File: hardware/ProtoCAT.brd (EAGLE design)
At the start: 59.7 x 53.3 mm, 53 parts, among them U1 ARDUINO

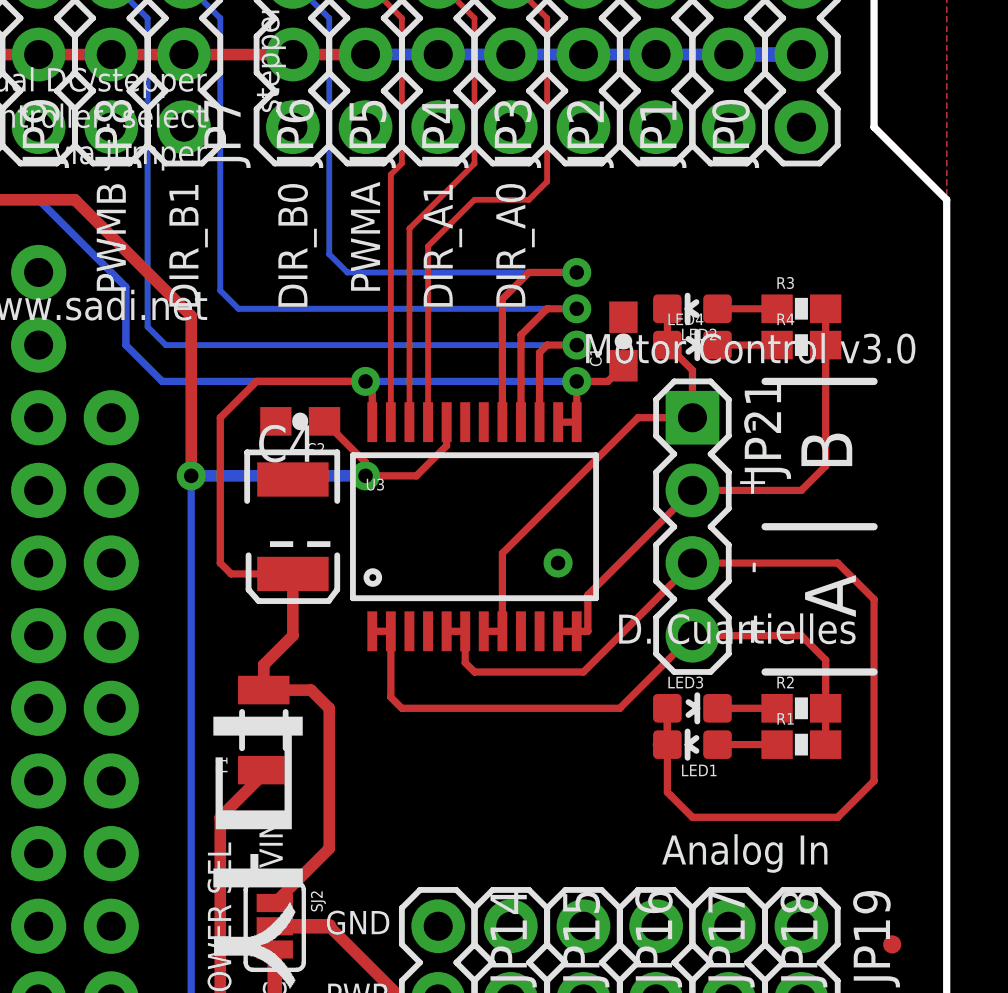
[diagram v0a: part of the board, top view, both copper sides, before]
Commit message: Removed unused layers
Removed unused layers and backup b# / s# files
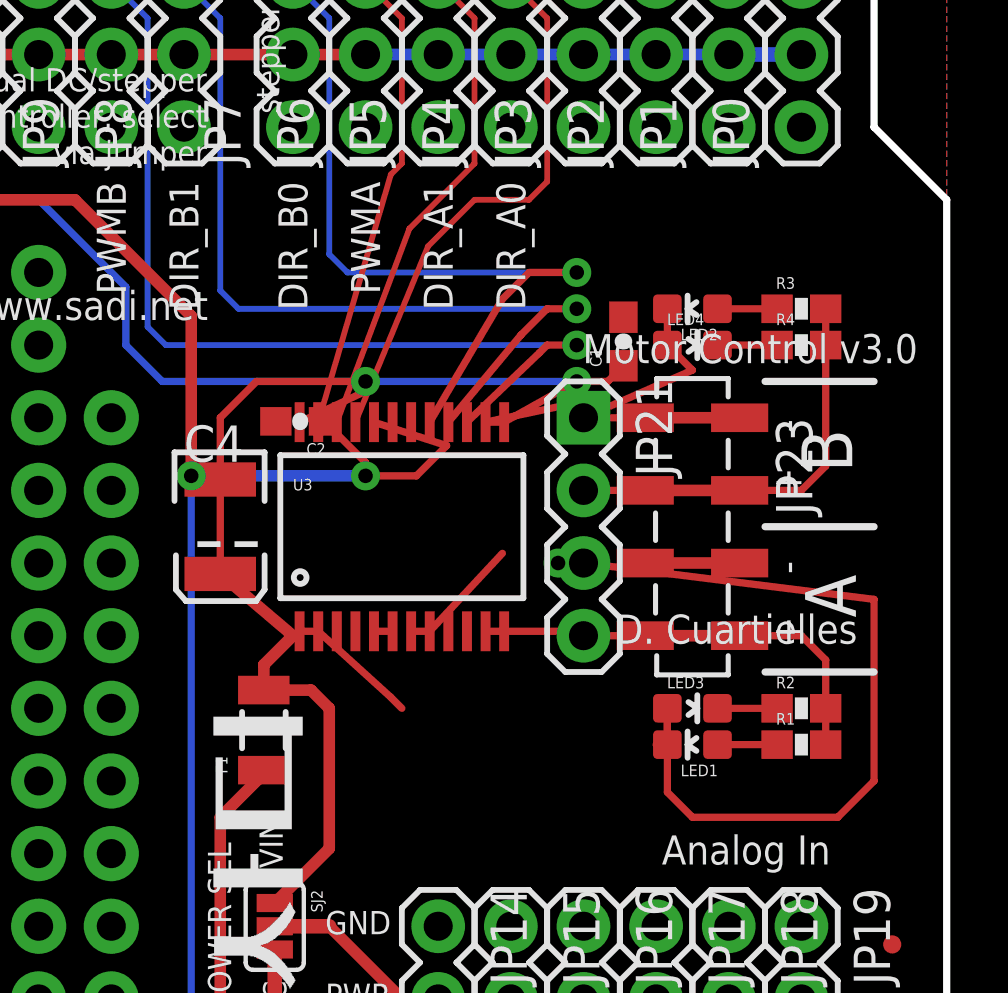
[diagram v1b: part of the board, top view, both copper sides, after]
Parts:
- added JP23: (no value), SparkFun-Connectors:1X04_SMD_STRAIGHT_COMBO
- U3: value (none) -> TB6612FNG
- moved JP21 3.81 mm to (47.0, 30.5)
- moved C4 2.54 mm to (34.3, 26.7)
- moved U3 2.54 mm to (40.6, 26.7)
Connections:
- net AOUT1: now also JP23.4
- net AOUT2: now also JP23.3
- net BOUT1: now also JP23.2
- net BOUT2: now also JP23.1
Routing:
- net AOUT2: track 37.1 -> 29.7 mm
- net AOUT1: track 23.0 -> 16.7 mm
- net FUSED_VIN: track 85.4 -> 90.0 mm
- net BOUT2: track 16.2 -> 12.9 mm
- net FUSED_VCC: track 73.4 -> 75.3 mm
- net PWMB: track 36.8 -> 37.9 mm
- net BIN2: track 34.5 -> 35.4 mm
- net BIN1: track 31.3 -> 32.0 mm
- net AIN1: track 23.8 -> 24.3 mm
